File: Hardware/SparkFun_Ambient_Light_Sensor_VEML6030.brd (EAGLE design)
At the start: 25.4 x 25.4 mm, 43 parts, among them U1 VEML6030

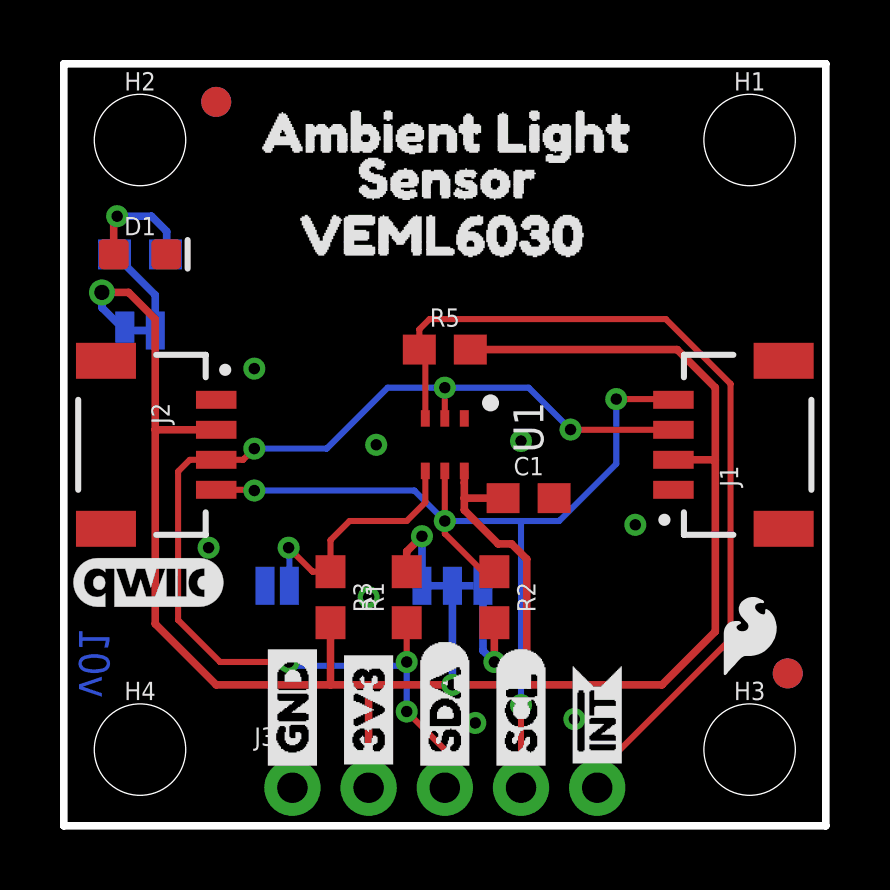
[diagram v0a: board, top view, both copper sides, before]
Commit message: Routes 3.3V line on underside and data lines on the topside...
* Adds silk on the underside for address selection
* Adds power silk to LED
* moves resistor to top side
* Fixes GND net on 5 pin header
* Changes version to v10
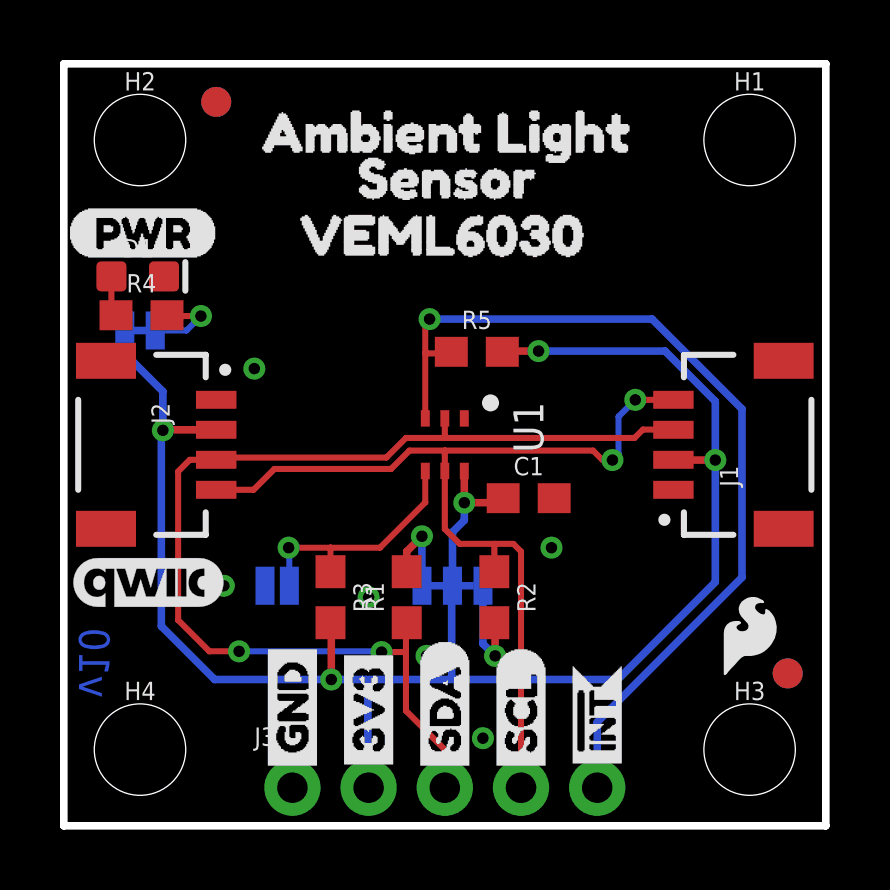
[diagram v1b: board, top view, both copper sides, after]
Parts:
- added U$19: (no value), Labels:PWR-()-04
- added U$20: (no value), Address text:ADDRESSES4
- added U$21: (no value), Address text:DEFAULT#2
- added U$22: (no value), Address text:0X481
- added U$23: (no value), Address text:JUMPER#3
- added U$24: (no value), Address text:0X103
- moved U$14 4.06 mm to (4.83, 18.5)
- moved R4 2.03 mm to (2.59, 17.0), flipped to the top
- moved R5 1.07 mm to (13.8, 15.8)
- moved D1 0.74 mm to (2.46, 18.3)
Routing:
- net 3.3V: track 72.8 -> 62.8 mm, vias 2 -> 5
- net N$1: track 3.96 -> 1.36 mm, vias 1 -> 0
- net SDA: track 38.6 -> 36.8 mm, vias 6 -> 2
- net !INT: track 29.8 -> 30.5 mm, vias 0 -> 1
- net N$2: track 3.10 -> 2.87 mm, vias 0 -> 1
- net SCL: track 31.8 -> 31.7 mm, vias 4 -> 2
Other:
- board text added: "v10"
- board text removed: "v01"

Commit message: Makes small adjustment to 3.3V traces
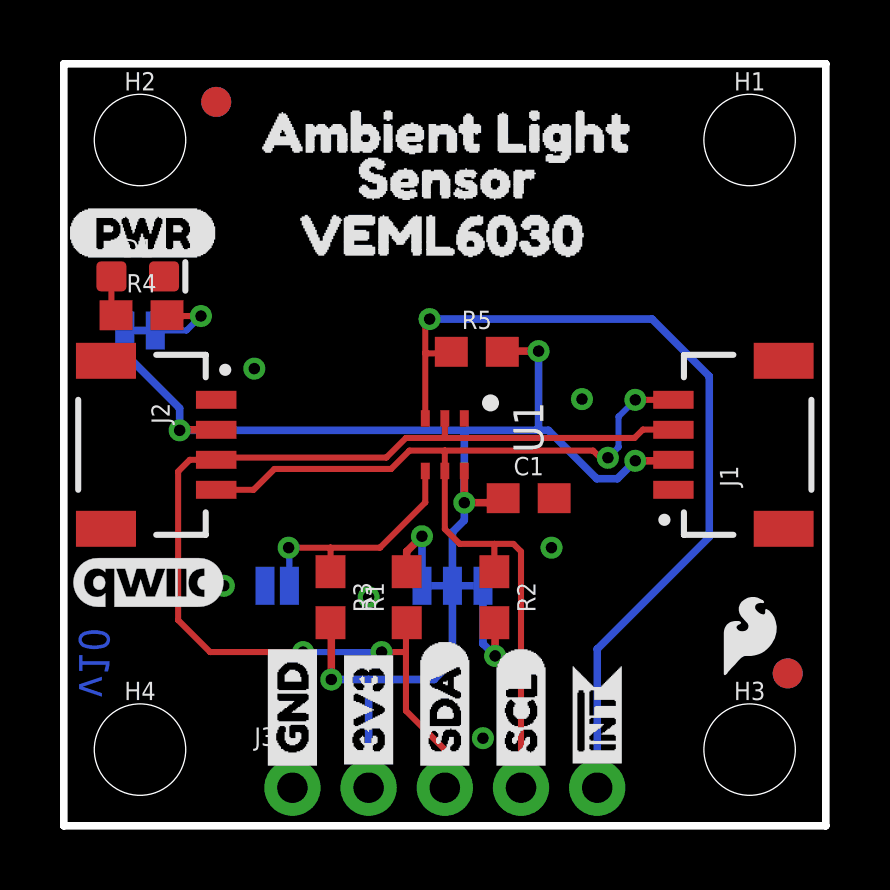
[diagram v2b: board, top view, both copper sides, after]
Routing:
- net 3.3V: track 62.8 -> 47.8 mm
- net !INT: track 30.5 -> 29.6 mm
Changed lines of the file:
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@@
 <drawing>
 <settings>
-<setting alwaysvectorfont="yes"/>
+<setting alwaysvectorfont="no"/>
 <setting verticaltext="up"/>
 </settings>
@@
 <via x="10.16" y="7.62" extent="1-16" drill="0.381"/>
 <via x="5.334" y="8.001" extent="1-16" drill="0.381"/>
-<via x="12.0904" y="5.6642" extent="1-16" drill="0.381"/>
 <via x="13.97" y="2.921" extent="1-16" drill="0.381"/>
+<via x="17.272" y="14.224" extent="1-16" drill="0.381"/>
 </signal>
 <signal name="3.3V">
@@
 <contactref element="R5" pad="2"/>
 <wire x1="10.16" y1="1.27" x2="10.16" y2="2.032" width="0.254" layer="16"/>
-<wire x1="18.4658" y1="4.8768" x2="21.717" y2="8.128" width="0.254" layer="16"/>
-<wire x1="21.717" y1="8.128" x2="21.717" y2="12.192" width="0.254" layer="16"/>
-<via x="21.717" y="12.192" extent="1-16" drill="0.381"/>
-<wire x1="21.717" y1="12.192" x2="20.328" y2="12.192" width="0.254" layer="1"/>
-<wire x1="20.328" y1="12.192" x2="20.32" y2="12.2" width="0.254" layer="1"/>
-<wire x1="3.2512" y1="13.1826" x2="3.2512" y2="6.6548" width="0.254" layer="16"/>
-<wire x1="3.2512" y1="13.1826" x2="3.302" y2="13.1826" width="0.254" layer="16"/>
-<via x="3.302" y="13.1826" extent="1-16" drill="0.381"/>
-<wire x1="3.302" y1="13.1826" x2="3.3194" y2="13.2" width="0.254" layer="1"/>
-<wire x1="3.3194" y1="13.2" x2="5.08" y2="13.2" width="0.254" layer="1"/>
+<via x="19.05" y="12.1666" extent="1-16" drill="0.381"/>
+<wire x1="20.32" y1="12.2" x2="20.2866" y2="12.1666" width="0.254" layer="1"/>
+<wire x1="20.2866" y1="12.1666" x2="19.05" y2="12.1666" width="0.254" layer="1"/>
+<wire x1="3.81" y1="13.1826" x2="3.8608" y2="13.1826" width="0.254" layer="16"/>
+<via x="3.8608" y="13.1826" extent="1-16" drill="0.381"/>
+<wire x1="3.8608" y1="13.1826" x2="3.8782" y2="13.2" width="0.254" layer="1"/>
+<wire x1="3.8782" y1="13.2" x2="5.08" y2="13.2" width="0.254" layer="1"/>
 <wire x1="2.032" y1="16.51" x2="2.032" y2="15.748" width="0.254" layer="16"/>
-<wire x1="3.302" y1="14.478" x2="2.032" y2="15.748" width="0.254" layer="16"/>
-<wire x1="3.302" y1="14.478" x2="3.302" y2="13.1826" width="0.254" layer="16"/>
+<wire x1="3.8608" y1="13.9192" x2="2.032" y2="15.748" width="0.254" layer="16"/>
+<wire x1="3.8608" y1="13.9192" x2="3.8608" y2="13.1826" width="0.254" layer="16"/>
 <wire x1="14.644" y1="10.922" x2="14.644" y2="11.088" width="0.254" layer="1"/>
 <wire x1="13.35" y1="11.83" x2="13.35" y2="10.7696" width="0.254" layer="1"/>
@@
 <wire x1="14.4916" y1="10.7696" x2="14.644" y2="10.922" width="0.254" layer="1"/>
 <wire x1="14.4916" y1="10.7696" x2="13.35" y2="10.7696" width="0.254" layer="1"/>
-<wire x1="10.1346" y1="1.2954" x2="10.1346" y2="4.826" width="0.254" layer="16"/>
-<wire x1="10.16" y1="1.27" x2="10.1346" y2="1.2954" width="0.254" layer="16"/>
-<wire x1="21.717" y1="12.192" x2="21.717" y2="14.1478" width="0.254" layer="16"/>
-<wire x1="21.717" y1="14.1478" x2="20.0406" y2="15.8242" width="0.254" layer="16"/>
-<wire x1="20.0406" y1="15.8242" x2="15.8242" y2="15.8242" width="0.254" layer="16"/>
+<wire x1="10.1346" y1="1.2954" x2="10.16" y2="1.27" width="0.254" layer="16"/>
 <via x="15.8242" y="15.8242" extent="1-16" drill="0.381"/>
 <wire x1="15.8242" y1="15.8242" x2="14.6422" y2="15.8242" width="0.254" layer="1"/>
@@
 <wire x1="8.9154" y1="6.7446" x2="8.9154" y2="4.8768" width="0.254" layer="1"/>
 <wire x1="12.954" y1="8.001" x2="12.9286" y2="7.9756" width="0.254" layer="16"/>
-<wire x1="12.9286" y1="7.9756" x2="12.9286" y2="4.953" width="0.254" layer="16"/>
-<wire x1="5.0292" y1="4.8768" x2="8.9154" y2="4.8768" width="0.254" layer="16"/>
-<wire x1="3.2512" y1="6.6548" x2="5.0292" y2="4.8768" width="0.254" layer="16"/>
-<wire x1="8.9154" y1="4.8768" x2="10.0838" y2="4.8768" width="0.254" layer="16"/>
-<wire x1="10.0838" y1="4.8768" x2="10.1346" y2="4.826" width="0.254" layer="16"/>
-<wire x1="10.1346" y1="4.826" x2="10.1854" y2="4.8768" width="0.254" layer="16"/>
-<wire x1="10.1854" y1="4.8768" x2="18.4658" y2="4.8768" width="0.254" layer="16"/>
-<wire x1="10.1854" y1="4.8768" x2="12.9286" y2="4.953" width="0" layer="19" extent="16-16"/>
+<wire x1="3.8608" y1="13.1826" x2="13.462" y2="13.1826" width="0.254" layer="16"/>
+<wire x1="13.462" y1="13.1826" x2="15.748" y2="13.1826" width="0.254" layer="16"/>
+<wire x1="15.748" y1="13.1826" x2="16.1544" y2="13.1826" width="0.254" layer="16"/>
+<wire x1="16.1544" y1="13.1826" x2="17.7673" y2="11.5697" width="0.254" layer="16"/>
+<wire x1="13.35" y1="10.7696" x2="13.35" y2="13.0706" width="0.254" layer="16"/>
+<wire x1="13.35" y1="13.0706" x2="13.462" y2="13.1826" width="0.254" layer="16"/>
+<wire x1="12.954" y1="5.4864" x2="12.954" y2="8.001" width="0.254" layer="16"/>
+<wire x1="8.9154" y1="4.8768" x2="10.16" y2="4.8768" width="0.254" layer="16"/>
+<wire x1="10.16" y1="4.8768" x2="10.16" y2="1.3208" width="0.254" layer="16"/>
+<wire x1="10.16" y1="1.3208" x2="10.1346" y2="1.2954" width="0.254" layer="16"/>
+<wire x1="10.16" y1="4.8768" x2="12.3444" y2="4.8768" width="0.254" layer="16"/>
+<wire x1="12.3444" y1="4.8768" x2="12.954" y2="5.4864" width="0.254" layer="16"/>
+<wire x1="19.05" y1="12.1666" x2="18.4531" y2="11.5697" width="0.254" layer="16"/>
+<wire x1="18.4531" y1="11.5697" x2="17.7673" y2="11.5697" width="0.254" layer="16"/>
+<wire x1="15.8242" y1="15.8242" x2="15.8242" y2="13.2588" width="0.254" layer="16"/>
+<wire x1="15.8242" y1="13.2588" x2="15.748" y2="13.1826" width="0.254" layer="16"/>
 </signal>
 <signal name="SCL">
@@
 <wire x1="6.326" y1="11.2" x2="7.0212" y2="11.8952" width="0.2032" layer="1"/>
 <wire x1="7.0212" y1="11.8952" x2="10.91001875" y2="11.8952" width="0.2032" layer="1"/>
-<wire x1="17.9578" y1="12.192" x2="18.288" y2="12.192" width="0.2032" layer="1"/>
-<wire x1="17.9578" y1="12.192" x2="17.643009375" y2="12.506790625" width="0.2032" layer="1"/>
-<via x="18.288" y="12.192" extent="1-16" drill="0.381"/>
-<wire x1="18.4912" y1="13.6398" x2="18.4912" y2="12.3952" width="0.2032" layer="16"/>
-<wire x1="18.288" y1="12.192" x2="18.4912" y2="12.3952" width="0.2032" layer="16"/>
+<wire x1="17.8816" y1="12.2682" x2="18.1356" y2="12.2682" width="0.2032" layer="1"/>
+<wire x1="17.8816" y1="12.2682" x2="17.643009375" y2="12.506790625" width="0.2032" layer="1"/>
+<via x="18.1356" y="12.2682" extent="1-16" drill="0.381"/>
+<wire x1="18.4912" y1="13.6398" x2="18.4912" y2="12.6238" width="0.2032" layer="16"/>
+<wire x1="18.1356" y1="12.2682" x2="18.4912" y2="12.6238" width="0.2032" layer="16"/>
 <wire x1="18.4912" y1="13.6398" x2="19.05" y2="14.1986" width="0.2032" layer="16"/>
 <wire x1="12.7" y1="12.506790625" x2="17.643009375" y2="12.506790625" width="0.2032" layer="1"/>
@@
 <wire x1="4.199" y1="12.2" x2="3.81" y2="11.811" width="0.2032" layer="1"/>
 <wire x1="3.81" y1="11.811" x2="3.81" y2="6.858" width="0.2032" layer="1"/>
-<wire x1="4.8514" y1="5.8166" x2="5.842" y2="5.8166" width="0.2032" layer="1"/>
-<wire x1="3.81" y1="6.858" x2="4.8514" y2="5.8166" width="0.2032" layer="1"/>
-<via x="5.842" y="5.8166" extent="1-16" drill="0.381"/>
+<wire x1="4.8768" y1="5.7912" x2="7.9756" y2="5.7912" width="0.2032" layer="1"/>
+<wire x1="3.81" y1="6.858" x2="4.8768" y2="5.7912" width="0.2032" layer="1"/>
+<via x="7.9756" y="5.7912" extent="1-16" drill="0.381"/>
 <wire x1="12.7" y1="2.54" x2="12.7" y2="1.27" width="0.2032" layer="1"/>
-<wire x1="11.4046" y1="3.8354" x2="12.7" y2="2.54" width="0.2032" layer="1"/>
-<wire x1="11.4046" y1="6.7446" x2="11.43" y2="6.77" width="0.2032" layer="1"/>
+<wire x1="12.7" y1="2.54" x2="11.4046" y2="3.8354" width="0.2032" layer="1"/>
 <wire x1="10.7522" y1="12.2762" x2="11.4046" y2="12.9286" width="0.2032" layer="1"/>
 <wire x1="5.08" y1="12.2" x2="5.1562" y2="12.2762" width="0.2032" layer="1"/>
@@
 <wire x1="12.7" y1="12.9286" x2="19.0246" y2="12.9286" width="0.2032" layer="1"/>
 <wire x1="12.7" y1="13.58" x2="12.7" y2="12.9286" width="0.2032" layer="1"/>
-<wire x1="11.4046" y1="6.7446" x2="11.4046" y2="5.7912" width="0.2032" layer="1"/>
-<wire x1="11.4046" y1="5.7912" x2="11.4046" y2="3.8354" width="0.2032" layer="1"/>
-<wire x1="10.5918" y1="5.7912" x2="10.5664" y2="5.8166" width="0.2032" layer="16"/>
-<wire x1="10.5664" y1="5.8166" x2="5.842" y2="5.8166" width="0.2032" layer="16"/>
+<wire x1="10.5918" y1="5.7912" x2="7.9756" y2="5.7912" width="0.2032" layer="16"/>
 <via x="10.5918" y="5.7912" extent="1-16" drill="0.381"/>
+<wire x1="11.4046" y1="3.8354" x2="11.4046" y2="5.7912" width="0.2032" layer="1"/>
+<wire x1="11.4046" y1="5.7912" x2="11.4046" y2="6.7446" width="0.2032" layer="1"/>
+<wire x1="11.4046" y1="6.7446" x2="11.43" y2="6.77" width="0.2032" layer="1"/>
 <wire x1="10.5918" y1="5.7912" x2="11.4046" y2="5.7912" width="0.2032" layer="1"/>
 </signal>
@@
 <contactref element="J3" pad="5"/>
 <contactref element="R5" pad="1"/>
-<wire x1="17.78" y1="1.27" x2="17.78" y2="3.4544" width="0.254" layer="16"/>
-<wire x1="17.78" y1="3.4544" x2="22.606" y2="8.2804" width="0.254" layer="16"/>
-<wire x1="22.606" y1="8.2804" x2="22.606" y2="13.8938" width="0.254" layer="16"/>
+<wire x1="17.78" y1="1.27" x2="17.78" y2="5.8928" width="0.254" layer="16"/>
+<wire x1="17.78" y1="5.8928" x2="21.5138" y2="9.6266" width="0.254" layer="16"/>
+<wire x1="21.5138" y1="9.6266" x2="21.5138" y2="14.986" width="0.254" layer="16"/>
 <wire x1="19.6088" y1="16.891" x2="12.192" y2="16.891" width="0.254" layer="16"/>
 <via x="12.192" y="16.891" extent="1-16" drill="0.381"/>
-<wire x1="22.606" y1="13.8938" x2="19.6088" y2="16.891" width="0.254" layer="16"/>
+<wire x1="21.5138" y1="14.986" x2="19.6088" y2="16.891" width="0.254" layer="16"/>
 <wire x1="12.05" y1="16.749" x2="12.192" y2="16.891" width="0.2032" layer="1"/>
 <wire x1="12.05" y1="13.58" x2="12.05" y2="15.748" width="0.2032" layer="1"/>
